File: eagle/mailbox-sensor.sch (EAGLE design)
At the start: 10 parts

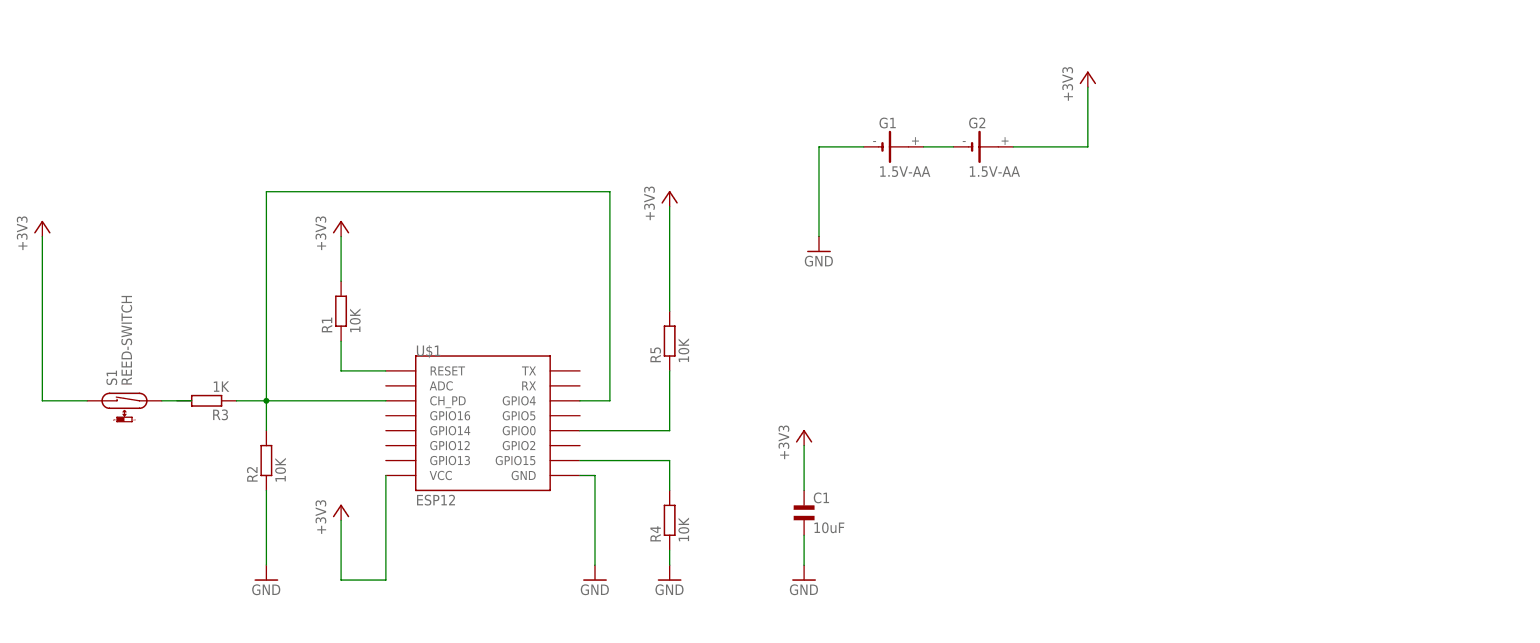
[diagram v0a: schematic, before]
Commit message: Added diod between RST and CH_PD
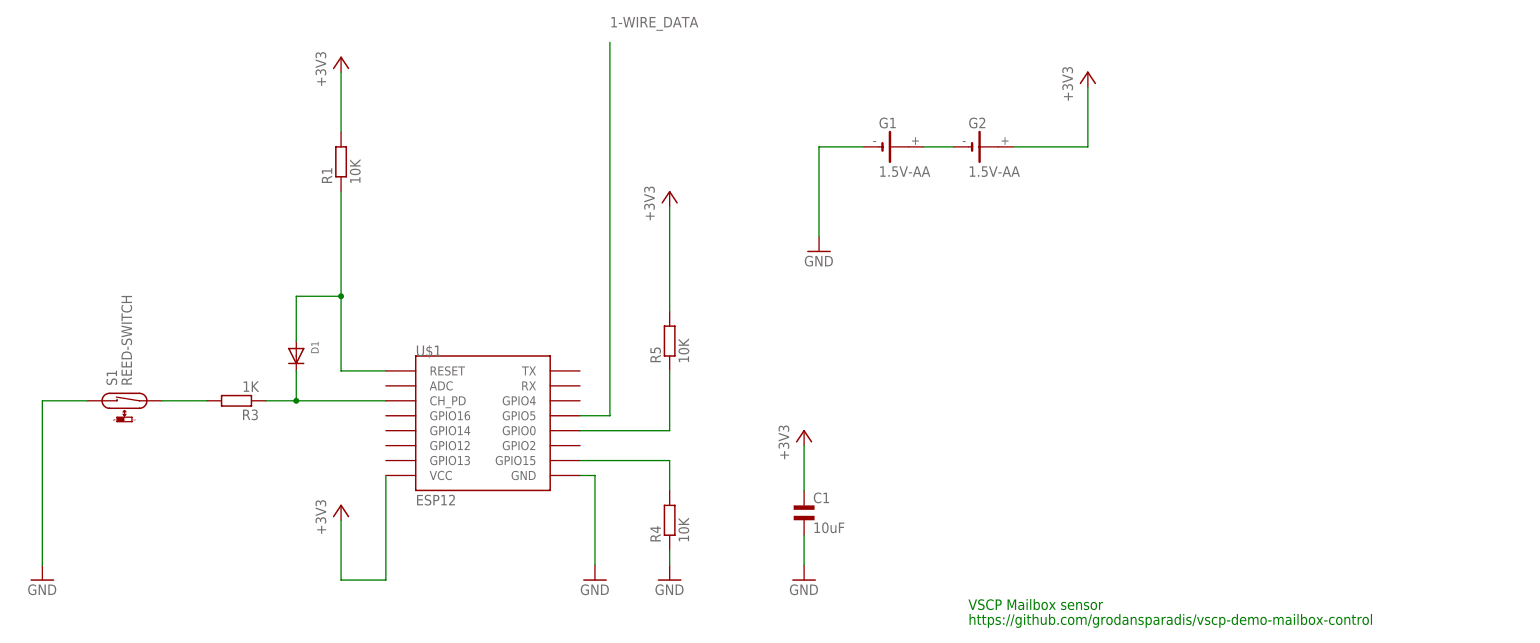
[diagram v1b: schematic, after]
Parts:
- removed R2: 10K, rcl:R-EU_M0805
- added D1: (no value), adafruit:DIODEDO-1N4148
- added U$2: VSCP_LOGO, VSCP_logo:VSCP_LOGO
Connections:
- new net 1-WIRE_DATA: U$1.GPIO5
- net +3V3: no longer S1.1
- net GND: now also S1.1; no longer R2.1
- net N$1: now also D1.C, R3.1, U$1.CH_PD; no longer R1.1, U$1.RESET
- net N$2: now also D1.A, R1.1, U$1.RESET; no longer R2.2, R3.1, U$1.CH_PD, U$1.GPIO4
- net N$6: now also R3.2
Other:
- note added: "VSCP Mailbox sensor"
- note added: "https://github.com/grodansparadis/vscp-demo-mailbox-control"
- moved on the sheet: R1, R3
